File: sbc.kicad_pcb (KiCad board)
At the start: 2 copper layers, 9 parts, among them J3 Conn_01x02_Pin, U1 TLV62568DBV, U3 MT41K256M16TW, U4 BQ24230RGT, U5 TLV62568DBV, U7 NCP1117-2.5_SOT223, U8 TLV62568DBV, Y1 ASE-xxxMHz

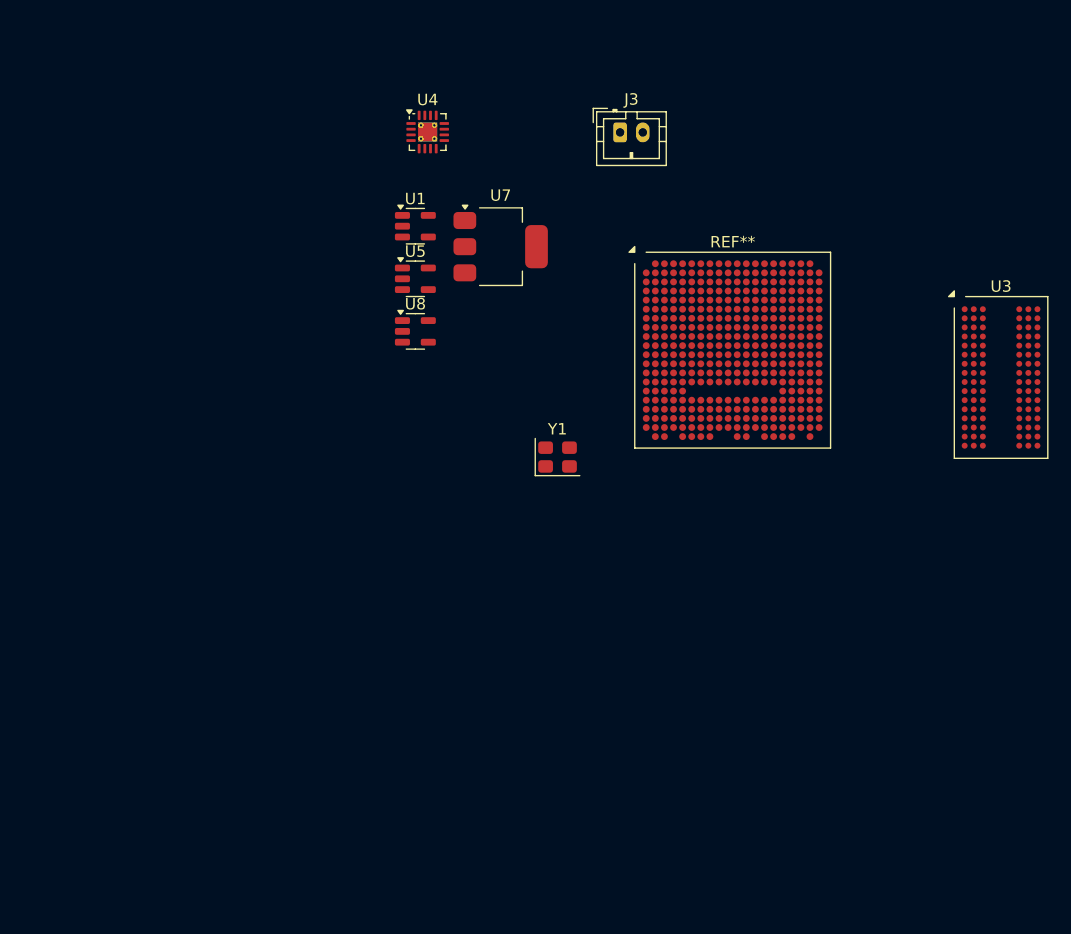
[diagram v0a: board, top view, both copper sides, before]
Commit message: Saving before changing RAM from DDR3 to Parallel SDR SRAM
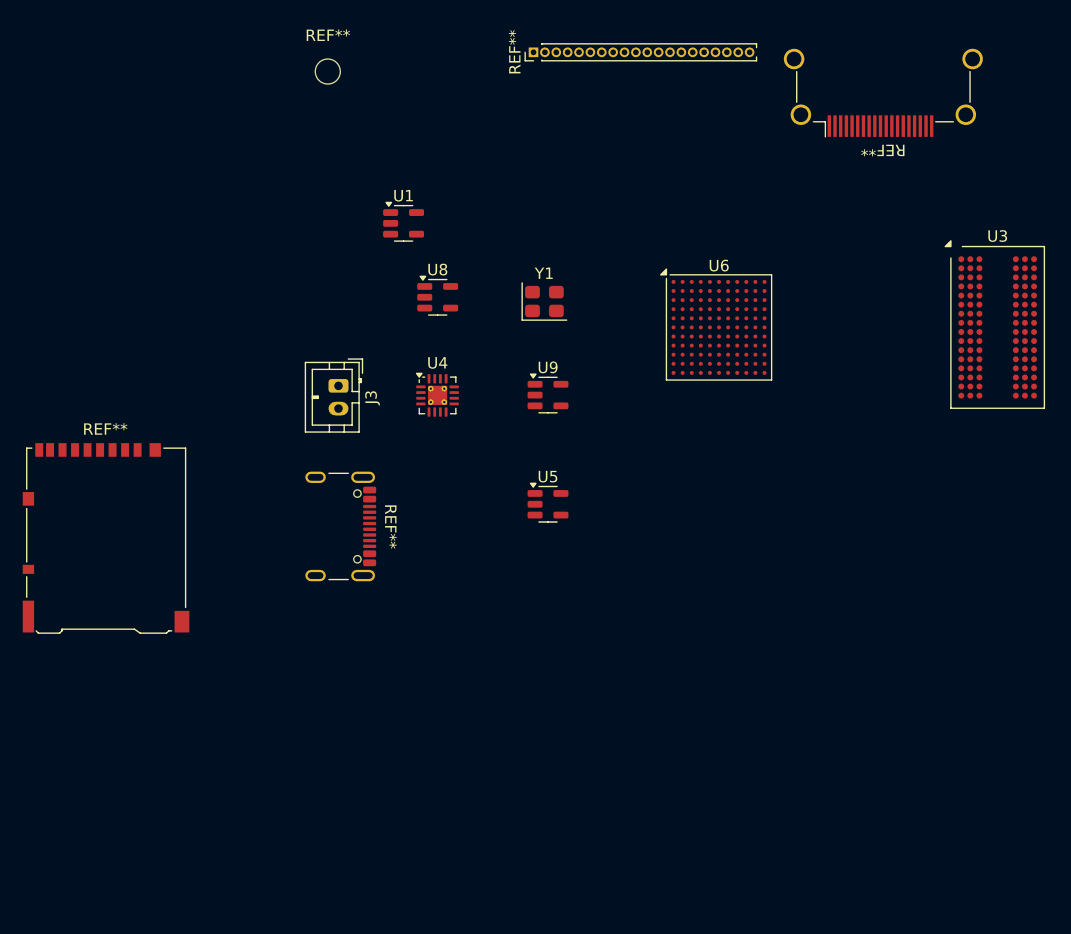
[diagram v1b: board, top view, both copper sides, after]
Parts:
- removed the REF** at (153.6, 79.0)
- removed U7: NCP1117-2.5_SOT223, Package_TO_SOT_SMD:SOT-223-3_TabPin2
- added REF**: USB_C_Receptacle_GCT_USB4105-xx-A_16P_TopMnt_Horizontal, Connector_USB:USB_C_Receptacle_GCT_USB4105-xx-A_16P_TopMnt_Horizontal, F.Cu at (118.0, 94.5)
- added REF**: PinHeader_1x20_P1.00mm_Vertical, Connector_PinHeader_1.00mm:PinHeader_1x20_P1.00mm_Vertical, F.Cu at (136.1, 52.8)
- added REF**: HDMI_A_Amphenol_10029449-x01xLF_Horizontal, Connector_Video:HDMI_A_Amphenol_10029449-x01xLF_Horizontal, F.Cu at (166.8, 54.3)
- added REF**: MountingHole_2.2mm_M2, MountingHole:MountingHole_2.2mm_M2, F.Cu at (118.0, 54.5)
- added REF**: microSD_HC_Hirose_DM3AT-SF-PEJM5, Connector_Card:microSD_HC_Hirose_DM3AT-SF-PEJM5, F.Cu at (98.5, 95.5)
- added U6: a, Package_BGA:BGA-121_9.0x9.0mm_Layout11x11_P0.8mm_Ball0.4mm_Pad0.35mm_NSMD, F.Cu at (152.4, 77.0)
- added U9: PAM2305AAB250, Package_TO_SOT_SMD:TSOT-23-5, F.Cu at (137.4, 83.0)
- moved J3 33.3 mm to (118.9, 82.1), turned to -90 degrees
- moved U4 23.2 mm to (127.7, 83.0)
- moved U5 23.0 mm to (137.4, 92.5)
- moved Y1 13.7 mm to (137.1, 74.7)
- moved U3 4.41 mm to (176.9, 77.0)
- moved U8 3.58 mm to (127.7, 74.3)
- moved U1 1.07 mm to (124.7, 67.8)

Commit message: Power routed. Saving before reworking ICE40 pins to optimize layout
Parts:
- removed REF**: USB_C_Receptacle_GCT_USB4105-xx-A_16P_TopMnt_Horizontal, Connector_USB:USB_C_Receptacle_GCT_USB4105-xx-A_16P_TopMnt_Horizontal
- removed REF**: PinHeader_1x20_P1.00mm_Vertical, Connector_PinHeader_1.00mm:PinHeader_1x20_P1.00mm_Vertical
- removed REF**: HDMI_A_Amphenol_10029449-x01xLF_Horizontal, Connector_Video:HDMI_A_Amphenol_10029449-x01xLF_Horizontal
- removed REF**: MountingHole_2.2mm_M2, MountingHole:MountingHole_2.2mm_M2
- removed REF**: microSD_HC_Hirose_DM3AT-SF-PEJM5, Connector_Card:microSD_HC_Hirose_DM3AT-SF-PEJM5
- removed U5: TLV62568DBV, Package_TO_SOT_SMD:SOT-23-5
- added C1: 100nF, Capacitor_SMD:C_0603_1608Metric, B.Cu at (120.1, 87.4)
- added C10: 10uF, Capacitor_SMD:C_0603_1608Metric, F.Cu at (125.4, 112.0)
- added C11: 100nF, Capacitor_SMD:C_0603_1608Metric, B.Cu at (138.2, 112.3)
- added C12: 10nF, Capacitor_SMD:C_0603_1608Metric, B.Cu at (141.2, 107.9)
- added C13: 4.7uF, Capacitor_SMD:C_0603_1608Metric, F.Cu at (172.9, 107.6)
- added C14: 0.01uF, Capacitor_SMD:C_0603_1608Metric, F.Cu at (129.3, 108.3)
- added C15: 100nF, Capacitor_SMD:C_0603_1608Metric, F.Cu at (175.1, 105.4)
- added C16: 10uF, Capacitor_SMD:C_0603_1608Metric, F.Cu at (108.4, 90.7)
- added C17: 100nF, Capacitor_SMD:C_0603_1608Metric, B.Cu at (138.2, 89.5)
- added C18: 10nF, Capacitor_SMD:C_0603_1608Metric, B.Cu at (141.1, 95.4)
- added C19: 100nF, Capacitor_SMD:C_0603_1608Metric, B.Cu at (138.2, 91.0)
- added C2: 10uF, Capacitor_SMD:C_0603_1608Metric, B.Cu at (121.5, 87.4)
- added C20: 100nF, Capacitor_SMD:C_0603_1608Metric, B.Cu at (138.2, 92.5)
- added C21: 100nF, Capacitor_SMD:C_0603_1608Metric, B.Cu at (138.2, 93.9)
- added C22: 100nF, Capacitor_SMD:C_0603_1608Metric, B.Cu at (138.2, 95.4)
- added C23: 10nF, Capacitor_SMD:C_0603_1608Metric, B.Cu at (141.1, 89.5)
- added C24: 10nF, Capacitor_SMD:C_0603_1608Metric, B.Cu at (141.1, 93.9)
- added C25: 10nF, Capacitor_SMD:C_0603_1608Metric, B.Cu at (141.1, 92.5)
- added C26: 10nF, Capacitor_SMD:C_0603_1608Metric, B.Cu at (141.1, 91.0)
- added C27: 100nF, Capacitor_SMD:C_0603_1608Metric, B.Cu at (144.1, 93.9)
- added C28: 100nF, Capacitor_SMD:C_0603_1608Metric, B.Cu at (144.1, 95.4)
- added C29: 10nF, Capacitor_SMD:C_0603_1608Metric, B.Cu at (147.0, 95.4)
- added C3: 100nF, Capacitor_SMD:C_0603_1608Metric, B.Cu at (108.0, 122.4)
- added C30: 10nF, Capacitor_SMD:C_0603_1608Metric, B.Cu at (147.0, 93.9)
- added C31: 100nF, Capacitor_SMD:C_0603_1608Metric, B.Cu at (156.9, 87.7)
- added C32: 100nF, Capacitor_SMD:C_0603_1608Metric, B.Cu at (159.9, 87.7)
- added C33: 100nF, Capacitor_SMD:C_0603_1608Metric, F.Cu at (173.6, 97.8)
- added C34: 22uF, Capacitor_SMD:C_0603_1608Metric, F.Cu at (113.2, 92.4)
- added C35: 22uF, Capacitor_SMD:C_0603_1608Metric, F.Cu at (114.7, 92.4)
- added C36: 27pF, Capacitor_SMD:C_0603_1608Metric, F.Cu at (118.9, 97.5)
- added C37: 27pF, Capacitor_SMD:C_0603_1608Metric, F.Cu at (117.5, 97.5)
- added C38: 0.1uF, Capacitor_SMD:C_0603_1608Metric, F.Cu at (122.7, 108.3)
- added C39: 1uF, Capacitor_SMD:C_0603_1608Metric, F.Cu at (172.2, 97.8)
- added C4: 4.7uF, Capacitor_SMD:C_0603_1608Metric, F.Cu at (115.6, 111.9)
- added C40: 0.1uF, Capacitor_SMD:C_0603_1608Metric, F.Cu at (124.2, 108.3)
- added C41: 1uF, Capacitor_SMD:C_0603_1608Metric, F.Cu at (173.6, 105.4)
- added C42: 0.1uF, Capacitor_SMD:C_0603_1608Metric, F.Cu at (125.6, 108.3)
- added C43: 0.1uF, Capacitor_SMD:C_0603_1608Metric, F.Cu at (127.1, 108.3)
- added C44: 3.3uF, Capacitor_SMD:C_0603_1608Metric, F.Cu at (129.9, 95.5)
- added C45: 4.7uF, Capacitor_SMD:C_0603_1608Metric, F.Cu at (117.2, 120.8)
- added C46: 4.7uF, Capacitor_SMD:C_0603_1608Metric, B.Cu at (122.8, 98.9)
- added C47: 10nF, Capacitor_SMD:C_0603_1608Metric, B.Cu at (159.9, 86.3)
- added C48: 10nF, Capacitor_SMD:C_0603_1608Metric, B.Cu at (156.9, 86.3)
- added C49: 100nF, Capacitor_SMD:C_0603_1608Metric, B.Cu at (138.2, 107.9)
- added C5: 4.7uF, Capacitor_SMD:C_0603_1608Metric, F.Cu at (104.7, 106.1)
- added C50: 100nF, Capacitor_SMD:C_0603_1608Metric, B.Cu at (138.2, 109.3)
- added C51: 100nF, Capacitor_SMD:C_0603_1608Metric, B.Cu at (138.2, 110.8)
- added C52: 10nF, Capacitor_SMD:C_0603_1608Metric, B.Cu at (141.2, 112.3)
- added C53: 10nF, Capacitor_SMD:C_0603_1608Metric, B.Cu at (141.2, 110.8)
- added C54: 10nF, Capacitor_SMD:C_0603_1608Metric, B.Cu at (141.2, 109.3)
- added C55: 22nF, Capacitor_SMD:C_0603_1608Metric, F.Cu at (175.1, 97.8)
- added C56: 1uF, Capacitor_SMD:C_0603_1608Metric, F.Cu at (172.2, 105.4)
- added C57: 100n, Capacitor_SMD:C_0603_1608Metric, B.Cu at (121.4, 98.9)
- added C58: 4.7uF, Capacitor_SMD:C_0603_1608Metric, B.Cu at (121.4, 102.5)
- added C59: 100n, Capacitor_SMD:C_0603_1608Metric, B.Cu at (122.8, 102.5)
- added C6: 10uF, Capacitor_SMD:C_0603_1608Metric, F.Cu at (111.7, 106.1)
- added C60: 0.1uF, Capacitor_SMD:C_0603_1608Metric, F.Cu at (124.2, 91.0)
- added C62: 2.2uF, Capacitor_SMD:C_0603_1608Metric, B.Cu at (159.9, 84.8)
- added C63: 2.2uF, Capacitor_SMD:C_0603_1608Metric, B.Cu at (156.9, 84.8)
- added C64: 1uF, Capacitor_SMD:C_0603_1608Metric, F.Cu at (112.2, 115.9)
- added C7: 4.7uF, Capacitor_SMD:C_0603_1608Metric, F.Cu at (104.7, 97.0)
- added C8: 10uF, Capacitor_SMD:C_0603_1608Metric, F.Cu at (125.5, 120.5)
- added C9: 10uF, Capacitor_SMD:C_0603_1608Metric, F.Cu at (114.0, 99.5)
- added D2: LED, LED_SMD:LED_0603_1608Metric, F.Cu at (120.1, 115.6)
- added D3: SMLVN6RGB, LED_SMD:LED_ROHM_SMLVN6, F.Cu at (169.8, 113.4)
- added D4: LED, LED_SMD:LED_0603_1608Metric, F.Cu at (139.6, 117.2)
- added D6: LED, LED_SMD:LED_0603_1608Metric, F.Cu at (121.6, 115.6)
- added H1: MountingHole, MountingHole:MountingHole_2.2mm_M2, F.Cu at (104.1, 78.7)
- added H2: MountingHole, MountingHole:MountingHole_2.2mm_M2, F.Cu at (175.3, 78.7)
- added H3: MountingHole, MountingHole:MountingHole_2.2mm_M2, F.Cu at (175.3, 124.5)
- added H4: MountingHole, MountingHole:MountingHole_2.2mm_M2, F.Cu at (104.1, 124.5)
- added J1: USB_C_Receptacle_USB2.0_14P, Connector_USB:USB_C_Receptacle_JAE_DX07S016JA1R1500, F.Cu at (165.8, 79.7)
- added J2: Micro_SD_Card, Connector_Card:microSD_HC_Hirose_DM3BT-DSF-PEJS, B.Cu at (110.5, 89.0)
- added J4: Conn_01x06_Pin, Connector_PinHeader_2.54mm:PinHeader_1x06_P2.54mm_Vertical, F.Cu at (119.4, 124.5)
- added J5: Conn_01x14_Pin, Connector_PinHeader_2.54mm:PinHeader_1x14_P2.54mm_Vertical, F.Cu at (142.2, 78.7)
- added J6: USB_C_Receptacle_USB2.0_14P, Connector_USB:USB_C_Receptacle_JAE_DX07S016JA1R1500, F.Cu at (105.2, 116.2)
- added J7: USB_C_Receptacle_USB2.0_14P, Connector_USB:USB_C_Receptacle_JAE_DX07S016JA1R1500, F.Cu at (151.0, 79.7)
- added J8: Conn_01x14_Pin, Connector_PinHeader_2.54mm:PinHeader_1x14_P2.54mm_Vertical, F.Cu at (170.2, 124.5)
- added J9: Conn_01x04_Pin, Connector_PinHeader_1.00mm:PinHeader_1x04_P1.00mm_Vertical, F.Cu at (132.1, 93.0)
- added JP2: Jumper_2_Small_Open, Button_Switch_SMD:SW_DIP_SPSTx01_Slide_6.7x4.1mm_W6.73mm_P2.54mm_LowProfile_JPin, F.Cu at (132.9, 117.4)
- added L1: 2.2uH, Inductor_SMD:L_Neosid_SMS-ME3010, F.Cu at (109.8, 102.7)
- added L2: 2.2uH, Inductor_SMD:L_Neosid_SMS-ME3010, F.Cu at (112.7, 96.9)
- added L3: 2.2uH, Inductor_SMD:L_Neosid_SMS-ME3010, F.Cu at (105.9, 91.6)
- added L4: 600R, Inductor_SMD:L_0603_1608Metric, F.Cu at (172.9, 100.0)
- added L6: 2.2uH, Inductor_SMD:L_0603_1608Metric, F.Cu at (125.4, 113.5)
- added L7: 600, Inductor_SMD:L_0603_1608Metric, B.Cu at (124.3, 98.9)
- added L8: 600, Inductor_SMD:L_0603_1608Metric, B.Cu at (125.8, 102.5)
- added Q2: BSS84, Package_TO_SOT_SMD:SOT-23, F.Cu at (143.5, 117.8)
- added R1: 1M, Resistor_SMD:R_0603_1608Metric, B.Cu at (108.0, 110.0)
- added R10: 5.1k, Resistor_SMD:R_0603_1608Metric, F.Cu at (110.2, 113.7)
- added R11: 5.1k, Resistor_SMD:R_0603_1608Metric, F.Cu at (110.2, 118.8)
- added R12: 100k, Resistor_SMD:R_0603_1608Metric, F.Cu at (111.0, 99.5)
- added R13: 100k, Resistor_SMD:R_0603_1608Metric, F.Cu at (108.0, 99.5)
- added R16: 4.7k, Resistor_SMD:R_0603_1608Metric, F.Cu at (146.5, 110.0)
- added R17: 4.7k, Resistor_SMD:R_0603_1608Metric, F.Cu at (133.5, 112.0)
- added R18: 4.7k, Resistor_SMD:R_0603_1608Metric, F.Cu at (145.0, 110.0)
- added R19: 12k, Resistor_SMD:R_0603_1608Metric, B.Cu at (125.8, 98.9)
- added R2: 10k, Resistor_SMD:R_0603_1608Metric, B.Cu at (120.8, 91.1)
- added R20: 10k, Resistor_SMD:R_0603_1608Metric, B.Cu at (122.1, 104.7)
- added R21: 10k, Resistor_SMD:R_0603_1608Metric, F.Cu at (106.2, 106.1)
- added R22: 10k, Resistor_SMD:R_0603_1608Metric, F.Cu at (142.8, 107.8)
- added R23: 56k, Resistor_SMD:R_0603_1608Metric, F.Cu at (162.9, 84.8)
- added R24: 56k, Resistor_SMD:R_0603_1608Metric, F.Cu at (168.7, 84.8)
- added R25: 20R, Resistor_SMD:R_0603_1608Metric, F.Cu at (150.1, 89.8)
- added R26: 56k, Resistor_SMD:R_0603_1608Metric, F.Cu at (148.1, 84.8)
- added R27: 56k, Resistor_SMD:R_0603_1608Metric, F.Cu at (153.9, 84.8)
- added R29: 10k, Resistor_SMD:R_0603_1608Metric, F.Cu at (106.2, 97.0)
- added R3: 10k, Resistor_SMD:R_0603_1608Metric, B.Cu at (120.8, 92.5)
- added R31: 10k, Resistor_SMD:R_0603_1608Metric, F.Cu at (171.4, 109.0)
- added R32: 20R, Resistor_SMD:R_0603_1608Metric, F.Cu at (171.3, 117.4)
- added R33: 20R, Resistor_SMD:R_0603_1608Metric, F.Cu at (168.4, 117.4)
- added R34: 60R, Resistor_SMD:R_0603_1608Metric, F.Cu at (169.8, 117.4)
- added R35: 20R, Resistor_SMD:R_0603_1608Metric, F.Cu at (151.9, 89.8)
- added R36: 4.7k, Resistor_SMD:R_0603_1608Metric, F.Cu at (133.5, 110.5)
- added R37: 2.2k, Resistor_SMD:R_0603_1608Metric, F.Cu at (121.4, 94.9)
- added R38: 560k, Resistor_SMD:R_0603_1608Metric, F.Cu at (113.2, 89.5)
- added R39: 62k, Resistor_SMD:R_0603_1608Metric, F.Cu at (110.8, 88.7)
- added R4: 2.94k, Resistor_SMD:R_0603_1608Metric, F.Cu at (114.0, 114.5)
- added R40: 2.2k, Resistor_SMD:R_0603_1608Metric, F.Cu at (139.8, 107.8)
- added R41: 100R, Resistor_SMD:R_0603_1608Metric, F.Cu at (143.5, 115.1)
- added R42: 270R, Resistor_SMD:R_0603_1608Metric, F.Cu at (141.1, 117.2)
- added R43: 20R, Resistor_SMD:R_0603_1608Metric, F.Cu at (164.9, 89.8)
- added R44: 20R, Resistor_SMD:R_0603_1608Metric, F.Cu at (166.6, 89.8)
- added R45: 10k, Resistor_SMD:R_0603_1608Metric, B.Cu at (120.8, 83.7)
- added R46: 10k, Resistor_SMD:R_0603_1608Metric, B.Cu at (120.8, 85.2)
- added R47: 10k, Resistor_SMD:R_0603_1608Metric, B.Cu at (120.8, 89.6)
- added R48: 10k, Resistor_SMD:R_0603_1608Metric, F.Cu at (124.2, 92.5)
- added R49: 10k, Resistor_SMD:R_0603_1608Metric, F.Cu at (127.0, 94.9)
- added R5: 4.32k, Resistor_SMD:R_0603_1608Metric, F.Cu at (114.4, 116.7)
- added R50: 10k, Resistor_SMD:R_0603_1608Metric, F.Cu at (128.4, 94.9)
- added R53: 10k, Resistor_SMD:R_0603_1608Metric, F.Cu at (117.2, 119.3)
- added R54: 10k, Resistor_SMD:R_0603_1608Metric, F.Cu at (125.5, 119.1)
- added R55: 10k, Resistor_SMD:R_0603_1608Metric, F.Cu at (110.8, 94.3)
- added R6: 10k, Resistor_SMD:R_0603_1608Metric, F.Cu at (118.5, 111.9)
- added R7: 10k, Resistor_SMD:R_0603_1608Metric, F.Cu at (118.5, 113.4)
- added R8: 450k, Resistor_SMD:R_0603_1608Metric, F.Cu at (108.9, 110.0)
- added R9: 100k, Resistor_SMD:R_0603_1608Metric, F.Cu at (108.9, 108.6)
- added SW1: SW_Push, Button_Switch_SMD:SW_SPST_CK_RS282G05A3, F.Cu at (174.9, 113.2)
- added TP1V2: TestPoint_Flag, TestPoint:TestPoint_Keystone_5015_Micro_Mini, B.Cu at (173.6, 94.1)
- added TP2V5: TestPoint_Flag, TestPoint:TestPoint_Keystone_5015_Micro_Mini, B.Cu at (173.6, 91.4)
- added TP3V3: TestPoint_Flag, TestPoint:TestPoint_Keystone_5015_Micro_Mini, B.Cu at (173.6, 88.7)
- added TP5V0: TestPoint_Flag, TestPoint:TestPoint_Keystone_5015_Micro_Mini, B.Cu at (173.6, 86.0)
- added U10: PAM2305AAB250, Package_TO_SOT_SMD:TSOT-23-5, F.Cu at (125.5, 116.3)
- added U11: TLV62569DBV, Package_TO_SOT_SMD:SOT-23-5, F.Cu at (109.0, 106.1)
- added U12: MIC94093YC6, Package_TO_SOT_SMD:SOT-363_SC-70-6, F.Cu at (115.3, 89.4)
- added U14: NUP2202, Package_TO_SOT_SMD:SOT-363_SC-70-6, F.Cu at (165.8, 86.9)
- added U15: NUP2202, Package_TO_SOT_SMD:SOT-363_SC-70-6, F.Cu at (151.0, 86.9)
- added U2: a, Package_BGA:BGA-121_9.0x9.0mm_Layout11x11_P0.8mm_Ball0.4mm_Pad0.35mm_NSMD, F.Cu at (139.7, 101.6)
- added U7: 93LCxxBxxOT, Package_TO_SOT_SMD:SOT-23-6, F.Cu at (124.2, 94.9)
- added Y2: ASE-xxxMHz, Oscillator:Oscillator_SMD_Abracon_ASE-4Pin_3.2x2.5mm, F.Cu at (132.1, 108.1)
- U3: value MT41K256M16TW -> W25Q32JVSS; footprint Package_BGA:Micron_FBGA-96_8x14mm_Layout9x16_P0.8mm -> Package_SO:SOIC-8_5.3x5.3mm_P1.27mm
- U4: value BQ24230RGT -> TLV61070ADBV; footprint Package_DFN_QFN:VQFN-16-1EP_3x3mm_P0.5mm_EP1.68x1.68mm_ThermalVias -> Package_TO_SOT_SMD:SOT-23-6
- U6: value a -> AS6C1616; footprint Package_BGA:BGA-121_9.0x9.0mm_Layout11x11_P0.8mm_Ball0.4mm_Pad0.35mm_NSMD -> Package_SO:TSOP-I-48_18.4x12mm_P0.5mm
- U8: value TLV62568DBV -> FT2232HQ; footprint Package_TO_SOT_SMD:SOT-23-5 -> Package_DFN_QFN:QFN-64-1EP_9x9mm_P0.5mm_EP4.35x4.35mm
- U9: value PAM2305AAB250 -> BQ24230RGT; footprint Package_TO_SOT_SMD:TSOT-23-5 -> Package_DFN_QFN:VQFN-16-1EP_3x3mm_P0.5mm_EP1.68x1.68mm_ThermalVias
- Y1: value ASE-xxxMHz -> 12MHz; footprint Oscillator:Oscillator_SMD_Abracon_ASE-4Pin_3.2x2.5mm -> Crystal:Crystal_SMD_Abracon_ABM8AIG-4Pin_3.2x2.5mm
- moved U3 50.8 mm to (139.6, 111.5)
- moved J3 42.2 mm to (112.0, 123.7), turned to 0 degrees
- moved U9 39.1 mm to (117.2, 116.4), turned to 90 degrees
- moved U1 33.2 mm to (108.9, 97.0), turned to 180 degrees
- moved Y1 32.4 mm to (117.6, 100.6), turned to 180 degrees
- moved U8 27.5 mm to (125.0, 101.8)
- moved U6 26.0 mm to (160.7, 101.6)
- moved U4 18.9 mm to (110.8, 91.5), turned to 90 degrees
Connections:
- J3 pad 1: Net-(J3-Pin_1) -> V_BAT
- U1 pad 1: V_SYS -> EN
- U4 pad 2: Net-(J3-Pin_1) -> GND
- U4 pad 3: Net-(J3-Pin_1) -> EN
- U4 pad 4: V_SYS -> Net-(U4-V_{FB})
- U4 pad 5: V_SYS -> P5V
- U4 pad 6: GND -> V_SYS
- U8 pad 1: V_SYS -> GND
- U8 pad 2: GND -> Net-(U8-OSCI)
- U8 pad 3: Net-(U8-SW) -> Net-(U8-OSCO)
- U8 pad 4: V_SYS -> Net-(U8-VPHY)
- U8 pad 5: Net-(U8-FB) -> GND
- U9 pad 1: unconnected-(U9-Vin-Pad1) -> Net-(U9-TS)
- U9 pad 2: unconnected-(U9-GND-Pad2) -> V_BAT
- U9 pad 3: unconnected-(U9-EN-Pad3) -> V_BAT
- U9 pad 4: unconnected-(U9-FB-Pad4) -> GND
- U9 pad 5: unconnected-(U9-SW-Pad5) -> V_SYS
- Y1 pad 1: unconnected-(Y1-EN-Pad1) -> Net-(U8-OSCI)
- Y1 pad 2: GND -> Net-(U8-OSCO)
- Y1 pad 3: CLK -> (no net)
- Y1 pad 4: P3V3 -> (no net)
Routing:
- net GND: track 0.00 -> 62.1 mm, vias 0 -> 29
- net P3V3: track 0.00 -> 42.8 mm, vias 0 -> 16
- net /USB/1.8V: track 0.00 -> 29.4 mm
- net /USB/D1-: track 0.00 -> 25.9 mm, vias 0 -> 3
- net /USB/D1+: track 0.00 -> 23.5 mm, vias 0 -> 2
- net V_SYS: track 0.00 -> 23.4 mm, vias 0 -> 8
- net USB_VBUS2: track 0.00 -> 23.0 mm, vias 0 -> 2
- net USB_VBUS: track 0.00 -> 22.7 mm, vias 0 -> 3
- net P5V: track 0.00 -> 12.4 mm
- net EN: track 0.00 -> 12.1 mm
- net Net-(J6-SHIELD): track 0.00 -> 11.9 mm
- net /FPGA + SRAM/FPGA/SPI_CNFG_CS: track 0.00 -> 11.8 mm
- net V_BAT: track 0.00 -> 10.5 mm
- net Net-(U8-OSCO): track 0.00 -> 9.66 mm
- net /FPGA + SRAM/CDONE: track 0.00 -> 8.10 mm
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- added copper zone on B.Cu, net GND
- added copper zone on In1.Cu, net GND
- added copper zone on B.Cu, net P1V2
- added copper zone on In4.Cu, net P1V2
- added copper zone on B.Cu, net P2V5
- added copper zone on In4.Cu, net P2V5
- added copper zone on B.Cu, net P3V3
- added copper zone on In4.Cu, net P3V3
- added copper zone on In4.Cu, net P5V
- added copper zone on In4.Cu, net V_SYS
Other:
- board outline added: 76.2 x 50.8 mm
- copper layers 2 -> 6
- board text added: "VBAT 3.3V GND B10 B9 B8 B7 B6 B5 B4 B3 B2 B1 GND"
- board text added: "VBUS EN 5V T10 T9 T8 T7 T6 T5 T4 T3 T2 T1 GND"

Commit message: Finished board. Added BOM
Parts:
- added FB1: 600R, Capacitor_SMD:C_0603_1608Metric, B.Cu at (123.0, 87.4)
- moved C11 13.3 mm to (151.4, 113.4)
- moved C12 13.3 mm to (154.4, 109.0)
- moved C49 13.3 mm to (151.4, 109.0)
- moved C50 13.3 mm to (151.4, 110.5)
- moved C51 13.3 mm to (151.4, 111.9)
- moved C52 13.3 mm to (154.4, 113.4)
- moved C53 13.3 mm to (154.4, 111.9)
- moved C54 13.3 mm to (154.4, 110.5)
- moved R40 11.1 mm to (148.2, 115.1), turned to 0 degrees
- moved TP1V2 2.70 mm to (173.6, 91.4)
- moved TP2V5 2.70 mm to (173.6, 94.1)
- moved R41 1.77 mm to (145.3, 115.1), turned to 180 degrees
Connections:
- J9 pad 1: EXT_PLL1P -> EXT_PLL2P
- J9 pad 2: EXT_PLL1N -> EXT_PLL2N
- J9 pad 3: EXT_PLL2P -> EXT_PLL1P
- J9 pad 4: EXT_PLL2N -> EXT_PLL1N
- TP5V0 pad 1: P5V -> USB_VBUS2
- U2 pad A1: /FPGA + SRAM/IO_B8 -> /FPGA + SRAM/IO_T9
- U2 pad A10: /FPGA + SRAM/SD_DAT2 -> /FPGA + SRAM/FPGA/A13
- U2 pad A11: /FPGA + SRAM/SD_DAT3 -> /FPGA + SRAM/FPGA/A12
- U2 pad A2: /FPGA + SRAM/IO_B10 -> /FPGA + SRAM/IO_T7
- U2 pad A3: /FPGA + SRAM/IO_B9 -> /FPGA + SRAM/IO_T5
- U2 pad A4: /FPGA + SRAM/LED_B -> /FPGA + SRAM/IO_T3
- U2 pad A5: /FPGA + SRAM/IO_T2 -> /FPGA + SRAM/FPGA/A16
- U2 pad A6: /FPGA + SRAM/IO_T3 -> /FPGA + SRAM/FPGA/DQ15
- U2 pad A7: /FPGA + SRAM/IO_T6 -> /FPGA + SRAM/FPGA/DQ7
- U2 pad A8: /FPGA + SRAM/IO_T8 -> /FPGA + SRAM/FPGA/A15
- U2 pad A9: /FPGA + SRAM/SD_CLK -> /FPGA + SRAM/FPGA/A14
- U2 pad B1: /FPGA + SRAM/FPGA/DQ15 -> /FPGA + SRAM/USB2_DN
- U2 pad B11: /FPGA + SRAM/IO_B7 -> /FPGA + SRAM/FPGA/A10
- U2 pad B2: /FPGA + SRAM/FPGA/DQ14 -> /FPGA + SRAM/USB2_DP
- U2 pad B3: /FPGA + SRAM/USR_BTN1 -> /FPGA + SRAM/IO_T6
- U2 pad B4: /FPGA + SRAM/LED_G -> /FPGA + SRAM/IO_T4
- U2 pad B5: /FPGA + SRAM/IO_T1 -> /FPGA + SRAM/IO_T2
- U2 pad B6: /FPGA + SRAM/IO_T4 -> /FPGA + SRAM/IO_T1
- U2 pad B7: /FPGA + SRAM/IO_T5 -> /FPGA + SRAM/FPGA/DQ14
- U2 pad B8: /SD MMC/SD_CMD -> /FPGA + SRAM/FPGA/DQ6
- U2 pad B9: /FPGA + SRAM/SD_DAT0 -> /FPGA + SRAM/FPGA/A11
- U2 pad C1: /FPGA + SRAM/FPGA/DQ10 -> /FPGA + SRAM/IO_T10
- U2 pad C11: /FPGA + SRAM/FPGA/A0 -> /FPGA + SRAM/FPGA/A8
- U2 pad C2: /FPGA + SRAM/FPGA/DQ11 -> /FPGA + SRAM/IO_T8
- U2 pad C3: /FPGA + SRAM/FPGA/DQ12 -> /FPGA + SRAM/USB3_DP
- U2 pad C4: /FPGA + SRAM/FPGA/DQ13 -> /FPGA + SRAM/USB3_DN
- U2 pad C7: /FPGA + SRAM/IO_T7 -> /FPGA + SRAM/FPGA/DQ13
- U2 pad C8: /FPGA + SRAM/IO_T10 -> /FPGA + SRAM/FPGA/DQ5
- U2 pad C9: /FPGA + SRAM/SD_DAT1 -> /FPGA + SRAM/FPGA/A9
- U2 pad D1: /FPGA + SRAM/FPGA/DQ8 -> /FPGA + SRAM/FIFO7
- U2 pad D10: /FPGA + SRAM/FPGA/A1 -> /FPGA + SRAM/FPGA/A19
- U2 pad D11: /FPGA + SRAM/FPGA/A2 -> /FPGA + SRAM/FPGA/SRAM_WE_B
- U2 pad D2: /FPGA + SRAM/FPGA/DQ7 -> /FPGA + SRAM/FIFO_RXF_B
- U2 pad D3: /FPGA + SRAM/FPGA/DQ6 -> /FPGA + SRAM/SD_DAT0
- U2 pad D5: /FPGA + SRAM/LED_R -> /FPGA + SRAM/SD_DAT1
- U2 pad D7: /FPGA + SRAM/IO_T9 -> /FPGA + SRAM/FPGA/DQ12
- U2 pad D9: /FPGA + SRAM/FPGA/A4 -> /FPGA + SRAM/FPGA/DQ4
- U2 pad E1: /FPGA + SRAM/FPGA/DQ9 -> /FPGA + SRAM/FIFO5
- U2 pad E10: /FPGA + SRAM/FPGA/A7 -> /FPGA + SRAM/FPGA/SRAM_UB_B
- U2 pad E11: /FPGA + SRAM/FPGA/A3 -> /FPGA + SRAM/FPGA/SRAM_CE2
- U2 pad E2: /FPGA + SRAM/FPGA/DQ5 -> /FPGA + SRAM/FIFO6
- U2 pad E3: /FPGA + SRAM/FPGA/DQ4 -> /FPGA + SRAM/SD_CLK
- U2 pad E8: /FPGA + SRAM/FPGA/A5 -> /FPGA + SRAM/FPGA/DQ3
- U2 pad E9: /FPGA + SRAM/FPGA/A6 -> /FPGA + SRAM/FPGA/DQ11
- U2 pad F1: /FPGA + SRAM/FPGA/DQ3 -> /FPGA + SRAM/FIFO3
- U2 pad F10: /FPGA + SRAM/FPGA/A10 -> /FPGA + SRAM/FPGA/A18
- U2 pad F11: /FPGA + SRAM/FPGA/A8 -> /FPGA + SRAM/FPGA/SRAM_LB_B
- U2 pad F2: /FPGA + SRAM/FPGA/DQ2 -> /FPGA + SRAM/FIFO4
- U2 pad F3: /FPGA + SRAM/FPGA/DQ0 -> /FPGA + SRAM/SD_DAT3
- U2 pad F4: /FPGA + SRAM/FPGA/DQ1 -> /SD MMC/SD_CMD
- U2 pad F9: /FPGA + SRAM/FPGA/A9 -> /FPGA + SRAM/FPGA/DQ10
- U2 pad G10: /FPGA + SRAM/FPGA/A13 -> /FPGA + SRAM/FPGA/A7
- U2 pad G11: /FPGA + SRAM/FPGA/A11 -> /FPGA + SRAM/FPGA/A17
- U2 pad G2: /FPGA + SRAM/IO_B5 -> /FPGA + SRAM/FIFO2
- U2 pad G3: /FPGA + SRAM/IO_B4 -> /FPGA + SRAM/SD_DAT2
- U2 pad G8: /FPGA + SRAM/FPGA/A15 -> /FPGA + SRAM/FPGA/DQ9
- U2 pad G9: /FPGA + SRAM/FPGA/A12 -> /FPGA + SRAM/FPGA/DQ2
- U2 pad H1: /FPGA + SRAM/IO_B2 -> /FPGA + SRAM/FIFO0
- U2 pad H10: /FPGA + SRAM/FPGA/A17 -> /FPGA + SRAM/FPGA/A5
- U2 pad H11: /FPGA + SRAM/FPGA/A14 -> /FPGA + SRAM/FPGA/A6
- U2 pad H2: /FPGA + SRAM/IO_B1 -> /FPGA + SRAM/FIFO1
- U2 pad H3: /FPGA + SRAM/IO_B3 -> /FPGA + SRAM/FIFO_TXE_B
- U2 pad H7: /FPGA + SRAM/FIFO6 -> /FPGA + SRAM/FPGA/DQ8
- U2 pad H9: /FPGA + SRAM/FIFO_WR_B -> /FPGA + SRAM/FPGA/DQ1
- U2 pad J1: /FPGA + SRAM/USB2_DN -> /FPGA + SRAM/FIFO_WR_B
- U2 pad J10: /FPGA + SRAM/FPGA/A16 -> /FPGA + SRAM/FPGA/A3
- U2 pad J11: /FPGA + SRAM/FPGA/A19 -> /FPGA + SRAM/FPGA/A4
- U2 pad J2: /FPGA + SRAM/USB3_DP -> /FPGA + SRAM/LED_R
- U2 pad J3: /FPGA + SRAM/FPGA/SRAM_WE_B -> /FPGA + SRAM/LED_G
- U2 pad J4: /FPGA + SRAM/FPGA/SRAM_UB_B -> /FPGA + SRAM/USR_BTN1
- U2 pad J5: /FPGA + SRAM/FIFO1 -> /FPGA + SRAM/FIFO_RD_B
- U2 pad J7: /FPGA + SRAM/FIFO5 -> /FPGA + SRAM/FPGA/SRAM_OE_B
- U2 pad J8: /FPGA + SRAM/FIFO_RXF_B -> /FPGA + SRAM/FPGA/DQ0
- U2 pad K1: /FPGA + SRAM/USB2_DP -> /FPGA + SRAM/LED_B
- U2 pad K11: /FPGA + SRAM/FPGA/A18 -> /FPGA + SRAM/FPGA/A2
- U2 pad K2: /FPGA + SRAM/USB3_DN -> /FPGA + SRAM/IO_B8
- U2 pad K3: /FPGA + SRAM/FPGA/SRAM_CE2 -> /FPGA + SRAM/IO_B6
- U2 pad K4: /FPGA + SRAM/FIFO0 -> /FPGA + SRAM/IO_B4
- U2 pad K5: /FPGA + SRAM/FIFO2 -> /FPGA + SRAM/IO_B2
- U2 pad K6: /FPGA + SRAM/FIFO4 -> /FPGA + SRAM/IO_B1
- U2 pad K7: /FPGA + SRAM/FIFO7 -> /FPGA + SRAM/FPGA/SRAM_CE_B
- U2 pad L1: /FPGA + SRAM/FPGA/SRAM_OE_B -> /FPGA + SRAM/IO_B10
- U2 pad L2: /FPGA + SRAM/FPGA/SRAM_CE_B -> /FPGA + SRAM/IO_B9
- U2 pad L3: /FPGA + SRAM/FPGA/SRAM_LB_B -> /FPGA + SRAM/IO_B7
- U2 pad L4: /FPGA + SRAM/IO_B6 -> /FPGA + SRAM/IO_B5
- U2 pad L5: /FPGA + SRAM/FIFO3 -> /FPGA + SRAM/IO_B3
- U2 pad L7: /FPGA + SRAM/FIFO_TXE_B -> /FPGA + SRAM/FPGA/A0
- U2 pad L8: /FPGA + SRAM/FIFO_RD_B -> /FPGA + SRAM/FPGA/A1
- Y1 pad 3: (no net) -> Net-(U8-OSCO)
- Y1 pad 4: (no net) -> Net-(U8-OSCO)
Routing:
- net GND: track 62.1 -> 153.7 mm, vias 29 -> 74
- net P2V5: track 3.23 -> 82.7 mm, vias 0 -> 2
- net EN: track 12.1 -> 86.5 mm
- net /FPGA + SRAM/FPGA/SPI_CNFG_DI: track 0.00 -> 69.3 mm, vias 0 -> 2
- net P3V3: track 42.8 -> 111.4 mm, vias 16 -> 37
- net /FPGA + SRAM/FPGA/SPI_CNFG_SCK: track 3.77 -> 68.9 mm, vias 0 -> 2
- net P1V2: track 5.49 -> 63.3 mm, vias 2 -> 10
- net /FPGA + SRAM/FPGA/SPI_CNFG_DO: track 0.00 -> 52.5 mm, vias 0 -> 6
- net /FPGA + SRAM/LED_B: track 0.00 -> 45.2 mm, vias 0 -> 2
- net /FPGA + SRAM/LED_R: track 0.00 -> 43.2 mm, vias 0 -> 2
- net /FPGA + SRAM/USR_BTN1: track 0.00 -> 42.0 mm, vias 0 -> 2
- net /FPGA + SRAM/LED_G: track 0.00 -> 40.4 mm, vias 0 -> 2
- net /FPGA + SRAM/IO_B1: track 0.00 -> 37.8 mm, vias 0 -> 1
- net /FPGA + SRAM/IO_B2: track 0.00 -> 36.4 mm, vias 0 -> 1
- net USB_VBUS: track 22.7 -> 58.7 mm, vias 3 -> 4
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- added copper zone on In4.Cu, net USB_VBUS2
- removed copper zone on B.Cu, net GND
- removed copper zone on B.Cu, net P1V2
- removed copper zone on B.Cu, net P2V5
- removed copper zone on B.Cu, net P3V3
- removed copper zone on In4.Cu, net P5V
